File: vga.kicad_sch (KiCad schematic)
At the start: 51 parts, among them J21 Audio Header, J22 DB15_Female_HighDensity_Mount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, J23 Audio Out, J24 Component A/V, J31 Conn_01x20, U43 74LVC374, U44 74LS374

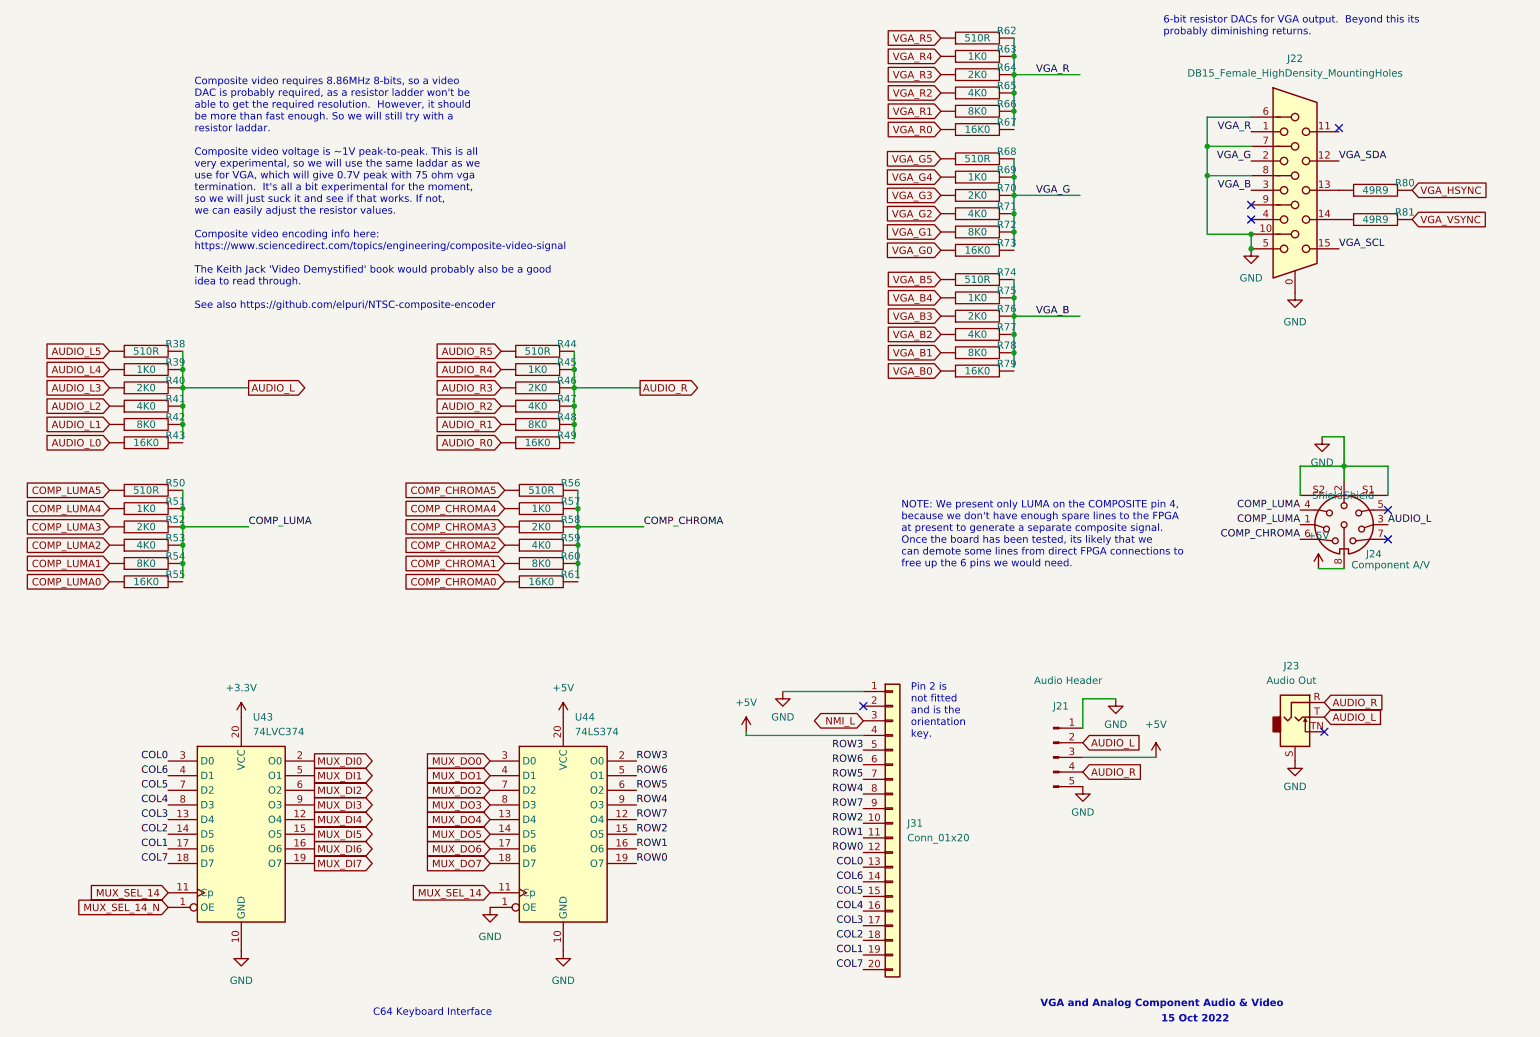
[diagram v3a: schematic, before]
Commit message: finish routing VGA connector
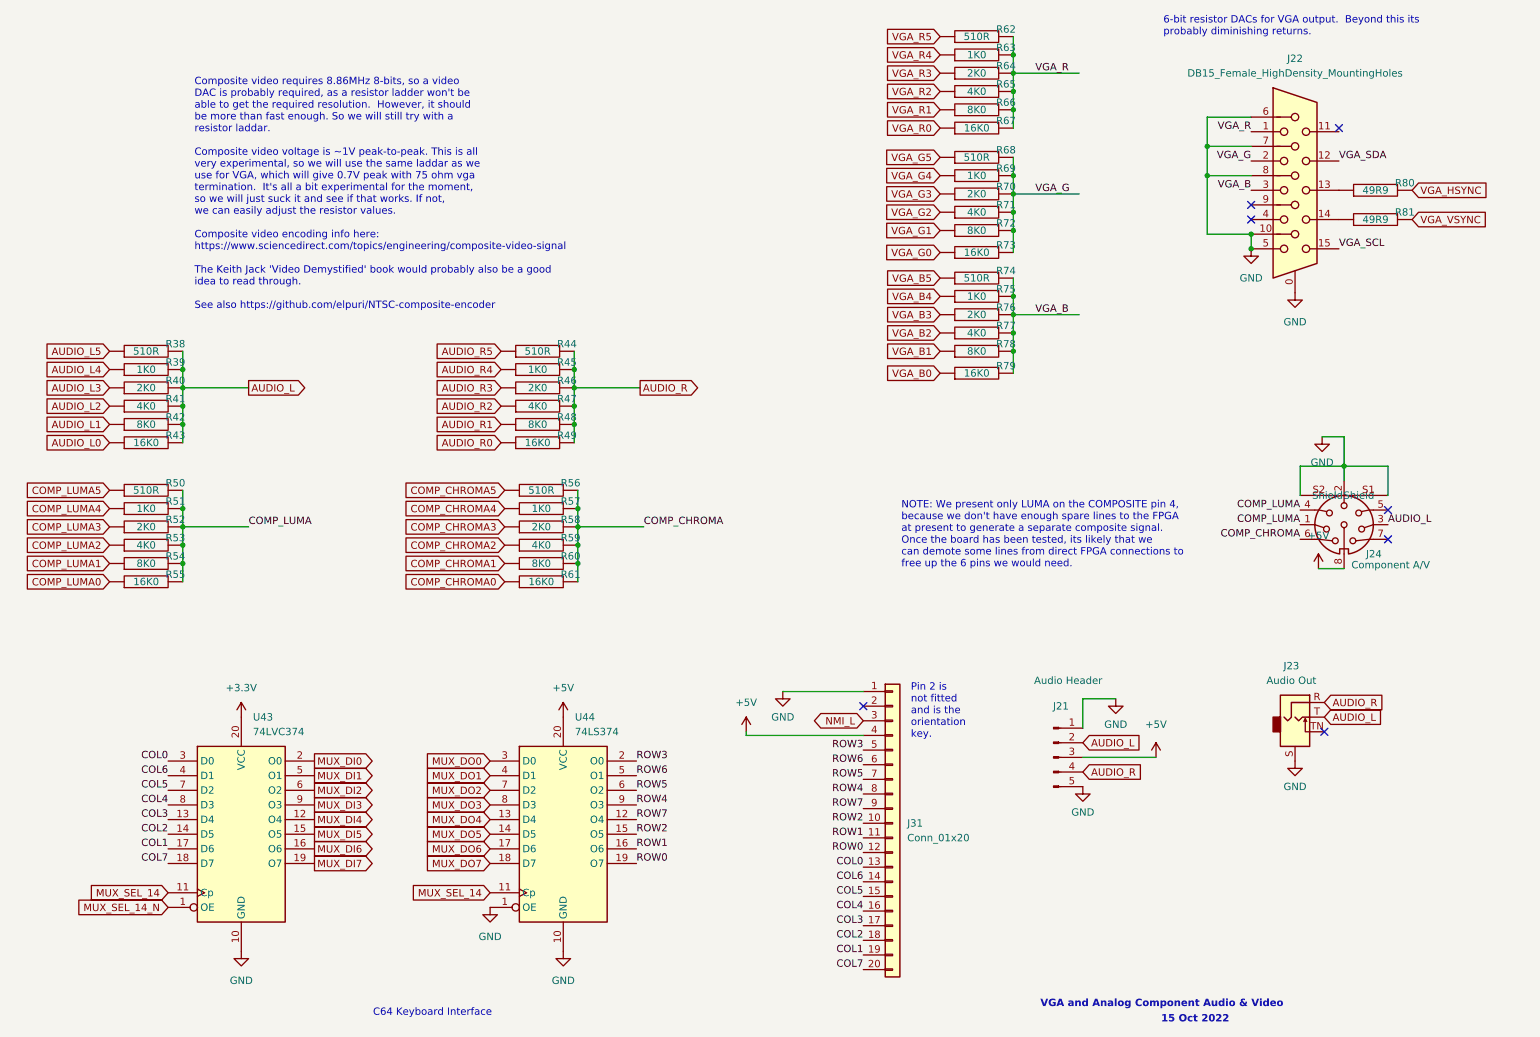
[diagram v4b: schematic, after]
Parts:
- R38, R39, R40, R41, R42, R43, R44, R45, R46, R47, R48, R49, R50, R51, R52, R53, R54, R55, R56, R57, R58, R59, R60, R61, R62, R63, R64, R65, R66, R67, R68, R69, R70, R71, R72, R73, R74, R75, R76, R77, R78, R79: footprint Resistor_THT:R_Box_L8.4mm_W2.5mm_P5.08mm -> snapeda:Labeled Resistor
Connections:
- net AUDIO_L: now also R43.2
- net AUDIO_R: now also R49.2
- net COMP_CHROMA: now also R61.2
- net COMP_LUMA: now also R55.2
- net VGA_B: now also R79.2
- net VGA_G: now also R73.2
- net VGA_R: now also R67.2

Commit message: add missing C64 keyboard footprint
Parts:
- J31: footprint (none) -> Connector_PinHeader_2.54mm:PinHeader_1x20_P2.54mm_Vertical
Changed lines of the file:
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@@
       (effects (font (size 1.27 1.27)) (justify left))
     )
-    (property "Footprint" "" (id 2) (at 166.37 159.385 0)
+    (property "Footprint" "Connector_PinHeader_2.54mm:PinHeader_1x20_P2.54mm_Vertical" (id 2) (at 166.37 159.385 0)
       (effects (font (size 1.27 1.27)) hide)
     )

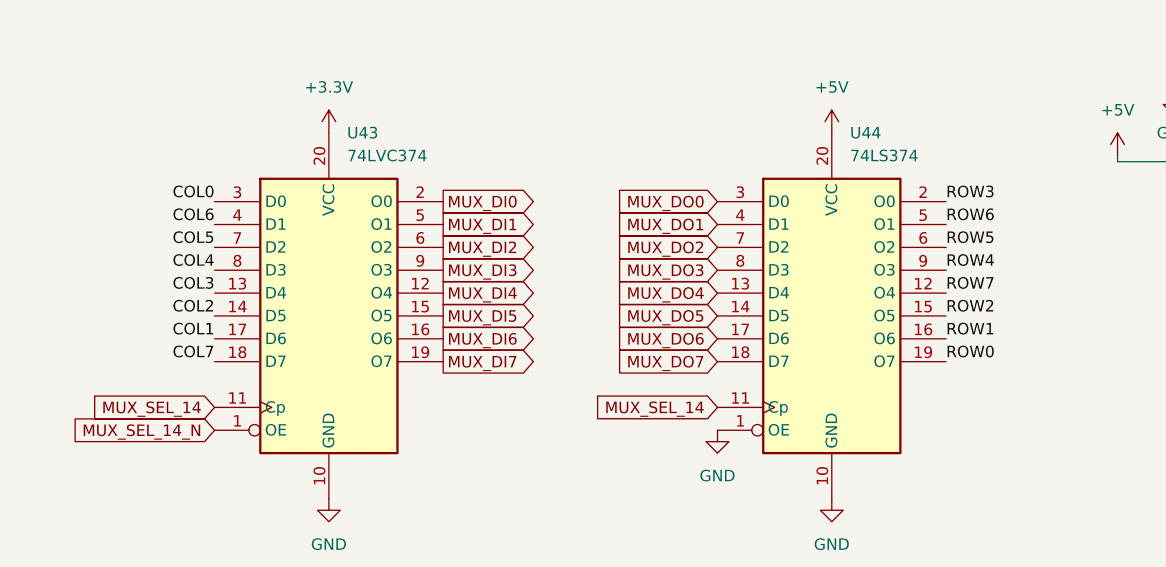
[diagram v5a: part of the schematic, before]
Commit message: route keyboard
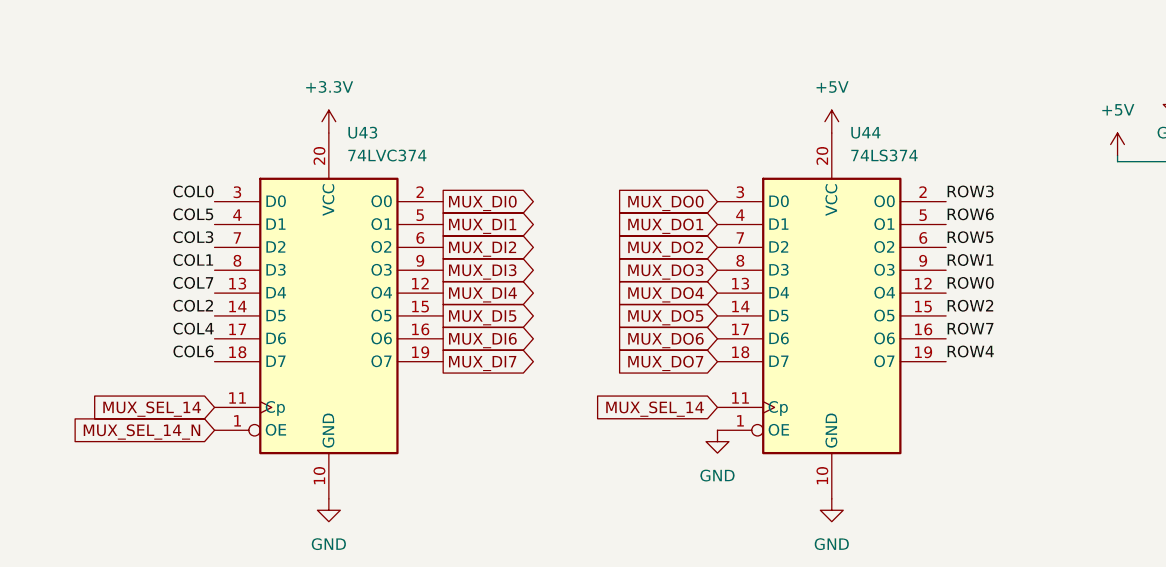
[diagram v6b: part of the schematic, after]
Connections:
- net COL1: now also U43.8 (D3); no longer U43.17 (D6)
- net COL3: now also U43.7 (D2); no longer U43.13 (D4)
- net COL4: now also U43.17 (D6); no longer U43.8 (D3)
- net COL5: now also U43.4 (D1); no longer U43.7 (D2)
- net COL6: now also U43.18 (D7); no longer U43.4 (D1)
- net COL7: now also U43.13 (D4); no longer U43.18 (D7)
- net ROW0: now also U44.12 (O4); no longer U44.19 (O7)
- net ROW1: now also U44.9 (O3); no longer U44.16 (O6)
- net ROW4: now also U44.19 (O7); no longer U44.9 (O3)
- net ROW7: now also U44.16 (O6); no longer U44.12 (O4)
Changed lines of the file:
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@@
     (effects (font (size 1.27 1.27)) (justify right bottom))
   )
-  (label "ROW1" (at 121.92 163.83 0)
+  (label "ROW1" (at 121.92 156.21 0)
     (effects (font (size 1.27 1.27)) (justify left bottom))
   )
@@
     (effects (font (size 1.27 1.27)) (justify right bottom))
   )
-  (label "COL7" (at 40.64 166.37 180)
+  (label "COL7" (at 40.64 158.75 180)
     (effects (font (size 1.27 1.27)) (justify right bottom))
   )
@@
     (effects (font (size 1.27 1.27)) (justify left bottom))
   )
-  (label "ROW0" (at 121.92 166.37 0)
+  (label "ROW0" (at 121.92 158.75 0)
     (effects (font (size 1.27 1.27)) (justify left bottom))
   )
@@
     (effects (font (size 1.27 1.27)) (justify left bottom))
   )
-  (label "COL6" (at 40.64 151.13 180)
+  (label "COL6" (at 40.64 166.37 180)
     (effects (font (size 1.27 1.27)) (justify right bottom))
   )
@@
     (effects (font (size 1.27 1.27)) (justify right bottom))
   )
-  (label "COL4" (at 40.64 156.21 180)
+  (label "COL4" (at 40.64 163.83 180)
     (effects (font (size 1.27 1.27)) (justify right bottom))
   )
@@
     (effects (font (size 1.27 1.27)) (justify right bottom))
   )
-  (label "ROW4" (at 121.92 156.21 0)
+  (label "ROW4" (at 121.92 166.37 0)
     (effects (font (size 1.27 1.27)) (justify left bottom))
   )
@@
     (effects (font (size 1.27 1.27)) (justify right bottom))
   )
-  (label "COL3" (at 40.64 158.75 180)
+  (label "COL3" (at 40.64 153.67 180)
     (effects (font (size 1.27 1.27)) (justify right bottom))
   )
@@
     (effects (font (size 1.27 1.27)) (justify left bottom))
   )
-  (label "COL1" (at 40.64 163.83 180)
+  (label "COL1" (at 40.64 156.21 180)
     (effects (font (size 1.27 1.27)) (justify right bottom))
   )
@@
     (effects (font (size 1.27 1.27)) (justify right bottom))
   )
-  (label "COL5" (at 40.64 153.67 180)
+  (label "COL5" (at 40.64 151.13 180)
     (effects (font (size 1.27 1.27)) (justify right bottom))
   )
@@
     (effects (font (size 1.27 1.27)) (justify left bottom))
   )
-  (label "ROW7" (at 121.92 158.75 0)
+  (label "ROW7" (at 121.92 163.83 0)
     (effects (font (size 1.27 1.27)) (justify left bottom))
   )

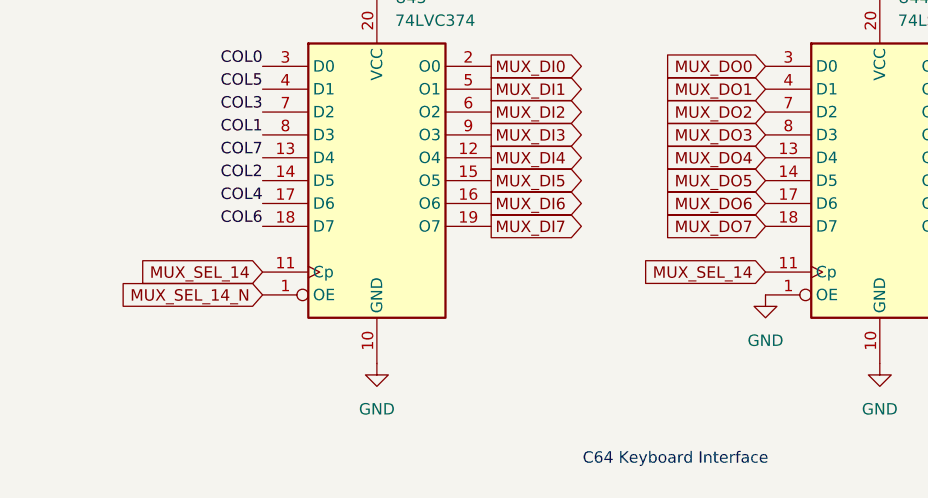
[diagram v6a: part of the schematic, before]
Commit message: renumber MUX registers to ease routing
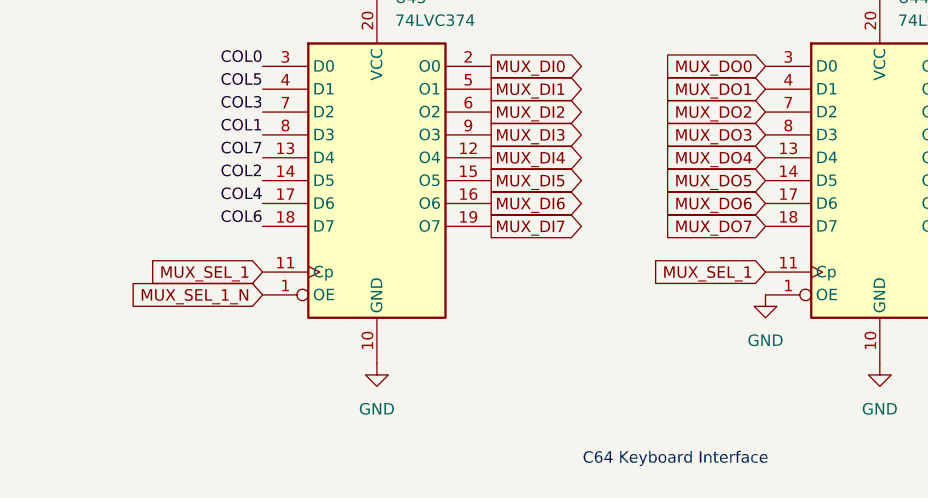
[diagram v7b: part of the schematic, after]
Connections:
- net MUX_SEL_14 renamed MUX_SEL_1
- net MUX_SEL_14_N renamed MUX_SEL_1_N
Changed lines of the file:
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@@
     )
   )
-  (global_label "MUX_SEL_14_N" (shape input) (at 40.64 173.99 180) (fields_autoplaced)
+  (global_label "MUX_SEL_1_N" (shape input) (at 40.64 173.99 180) (fields_autoplaced)
     (effects (font (size 1.27 1.27)) (justify right))
-    (property "Intersheet References" "${INTERSHEET_REFS}" (id 0) (at 24.1964 173.9106 0)
+    (property "Intersheet References" "${INTERSHEET_REFS}" (id 0) (at 25.4059 173.9106 0)
       (effects (font (size 1.27 1.27)) (justify right) hide)
     )
@@
     )
   )
-  (global_label "MUX_SEL_14" (shape input) (at 96.52 171.45 180) (fields_autoplaced)
+  (global_label "MUX_SEL_1" (shape input) (at 96.52 171.45 180) (fields_autoplaced)
     (effects (font (size 1.27 1.27)) (justify right))
-    (property "Intersheet References" "${INTERSHEET_REFS}" (id 0) (at 82.3745 171.3706 0)
+    (property "Intersheet References" "${INTERSHEET_REFS}" (id 0) (at 83.584 171.3706 0)
       (effects (font (size 1.27 1.27)) (justify right) hide)
     )
@@
     )
   )
-  (global_label "MUX_SEL_14" (shape input) (at 40.64 171.45 180) (fields_autoplaced)
+  (global_label "MUX_SEL_1" (shape input) (at 40.64 171.45 180) (fields_autoplaced)
     (effects (font (size 1.27 1.27)) (justify right))
-    (property "Intersheet References" "${INTERSHEET_REFS}" (id 0) (at 26.4945 171.3706 0)
+    (property "Intersheet References" "${INTERSHEET_REFS}" (id 0) (at 27.704 171.3706 0)
       (effects (font (size 1.27 1.27)) (justify right) hide)
     )

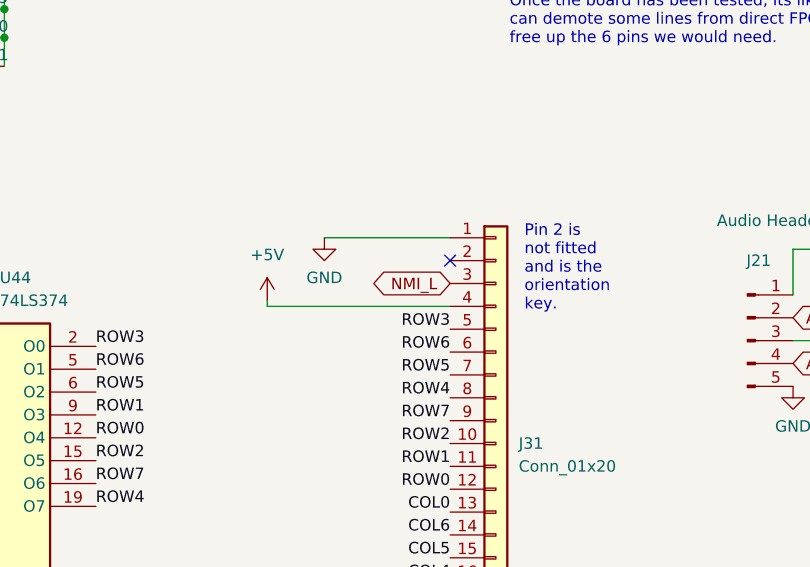
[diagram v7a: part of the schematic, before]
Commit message: plumb keyboard to MUX bus and fix RESTORE key label
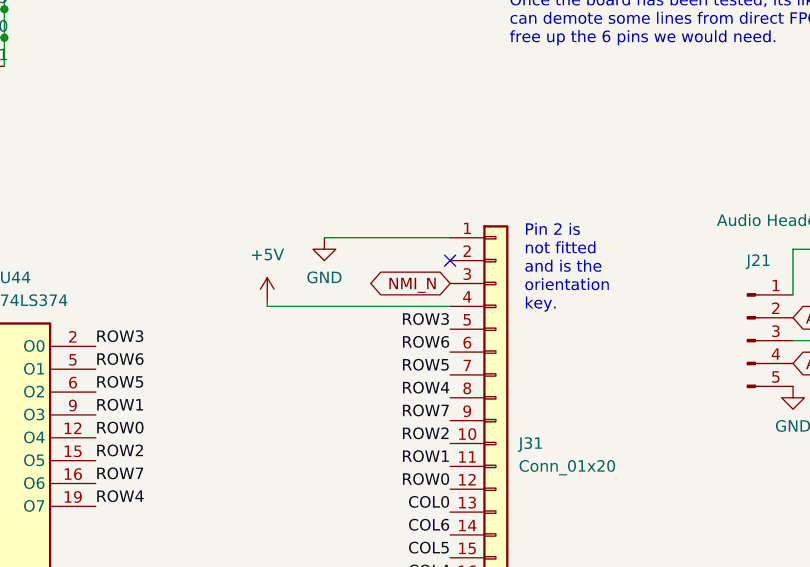
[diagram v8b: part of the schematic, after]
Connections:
- net NMI_L renamed NMI_N
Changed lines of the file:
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@@
     )
   )
-  (global_label "NMI_L" (shape bidirectional) (at 161.29 141.605 180) (fields_autoplaced)
+  (global_label "NMI_N" (shape bidirectional) (at 161.29 141.605 180) (fields_autoplaced)
     (effects (font (size 1.27 1.27)) (justify right))
-    (property "Intersheet References" "${INTERSHEET_REFS}" (id 0) (at 153.4945 141.5256 0)
+    (property "Intersheet References" "${INTERSHEET_REFS}" (id 0) (at 153.1921 141.5256 0)
       (effects (font (size 1.27 1.27)) (justify right) hide)
     )
